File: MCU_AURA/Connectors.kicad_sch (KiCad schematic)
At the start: 13 parts, among them J500 Screw_Terminal_01x04, J501 TSW-108-07-G-T, J502 532617006, J504 532617004, J505 532617004, U500 DMN6040SSD-13

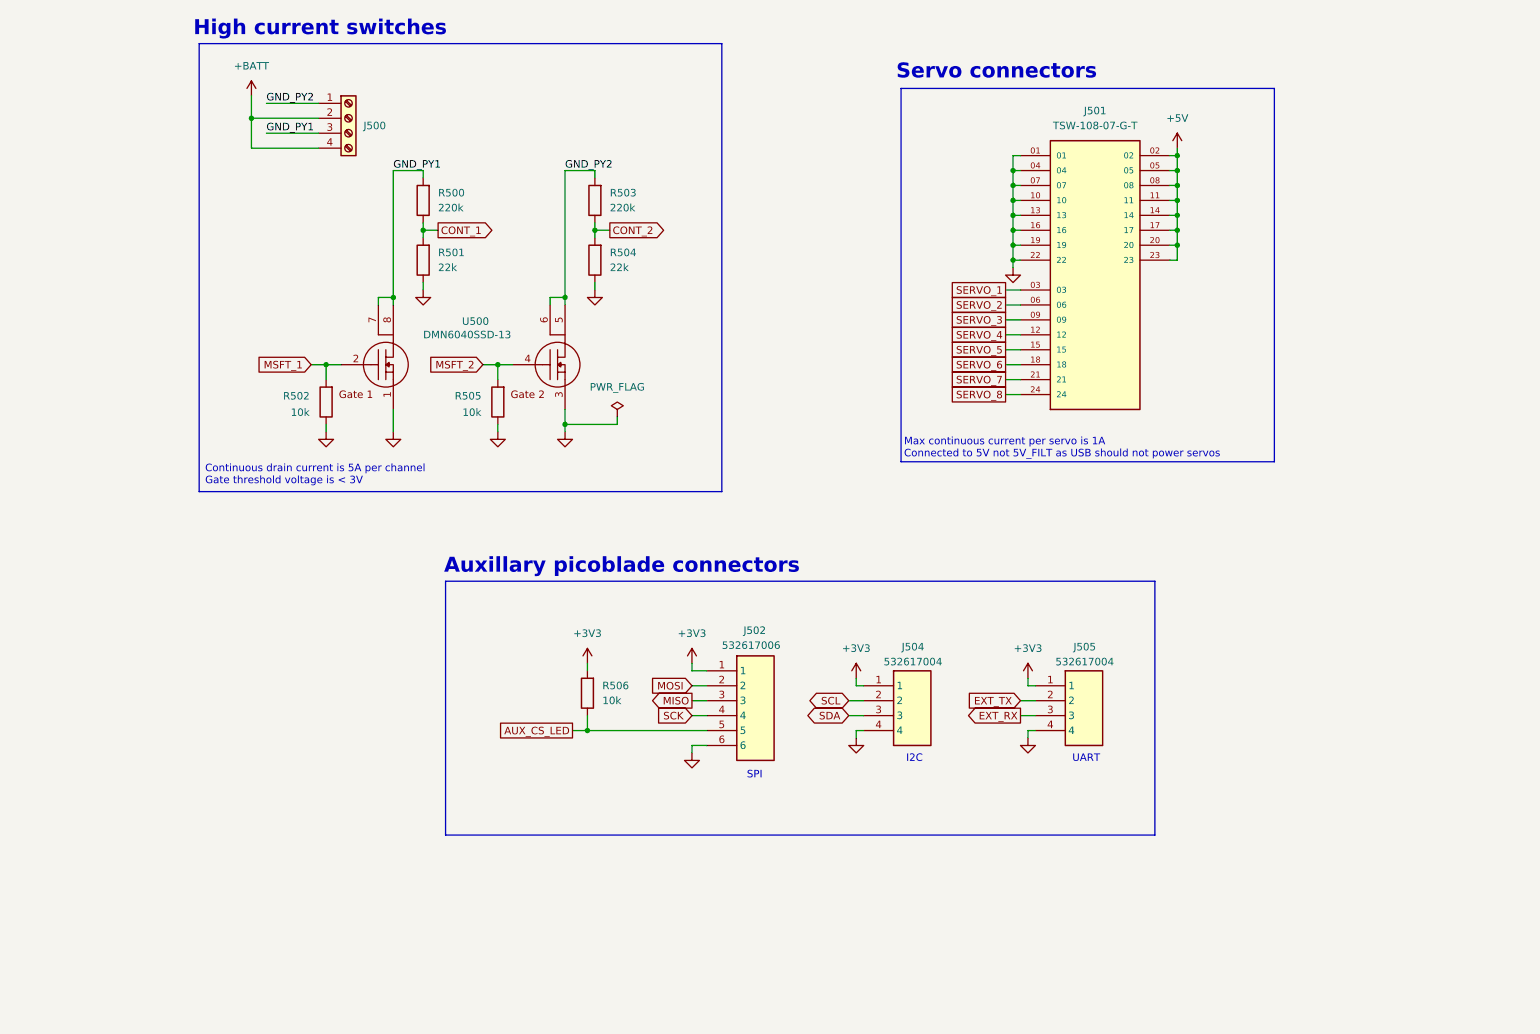
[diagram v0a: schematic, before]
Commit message: Started Editing
Problem syncing desktop to laptop (libraries).
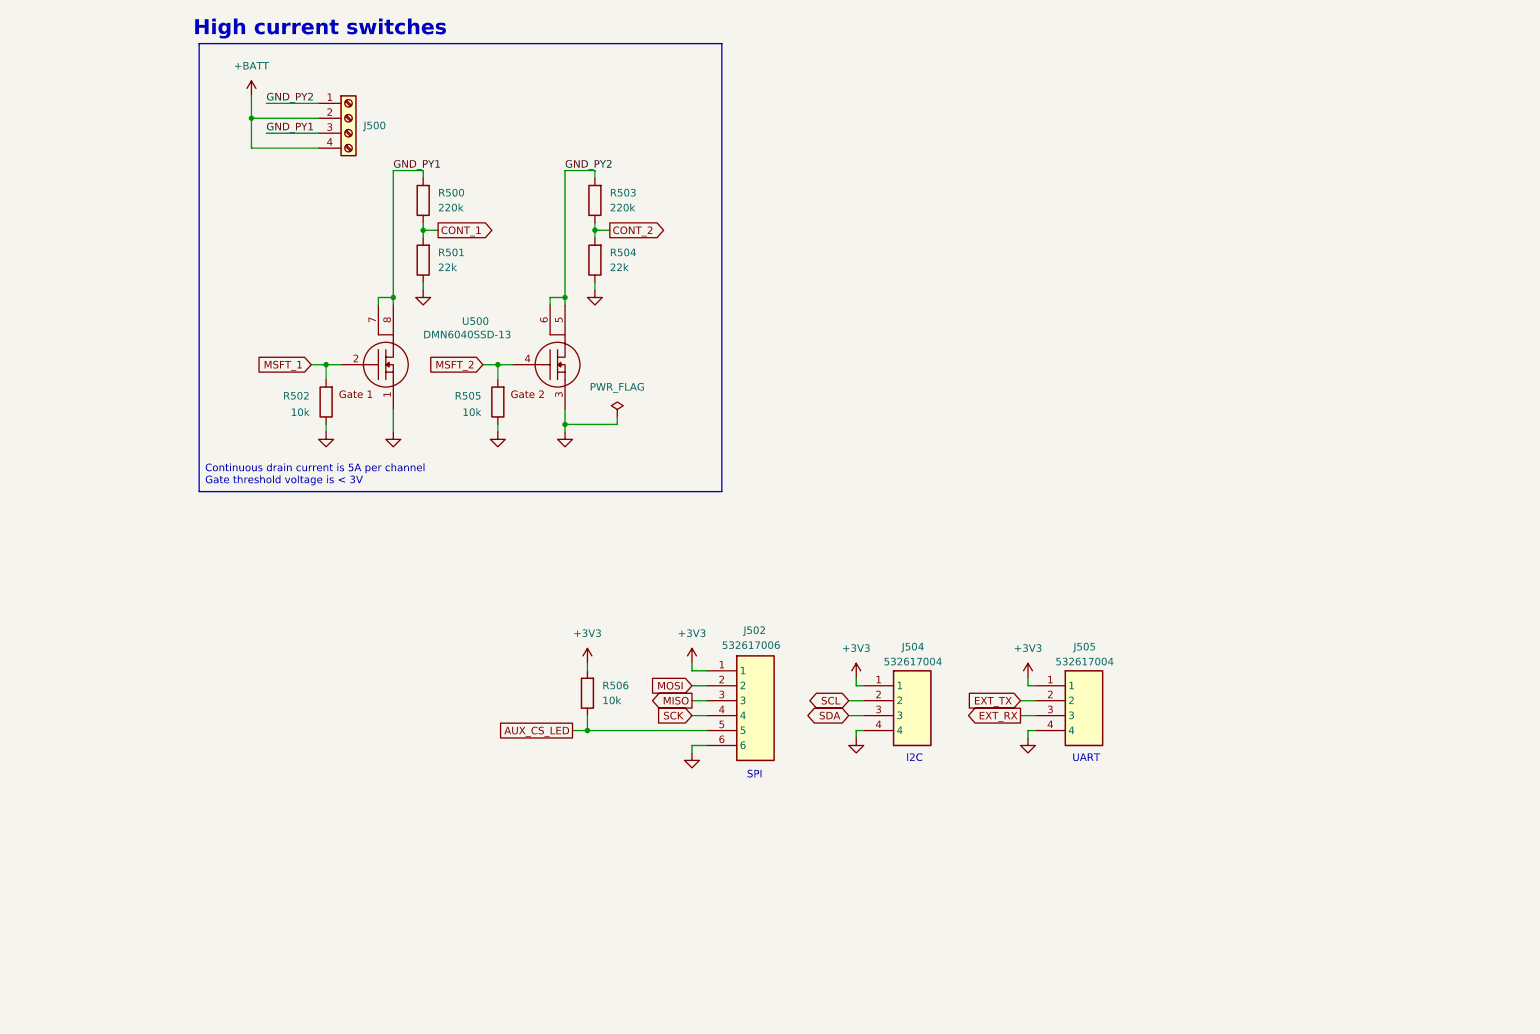
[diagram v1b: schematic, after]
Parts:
- removed J501: TSW-108-07-G-T, SAMTEC_TSW-108-07-G-T:SAMTEC_TSW-108-07-G-T, symbol TSW-108-07-G-T:TSW-108-07-G-T
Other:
- note removed: "Auxillary picoblade connectors"
- note removed: "Max continuous current per servo is 1A Connected to 5V not 5V_FILT as USB should not power servos"
- note removed: "Servo connectors"

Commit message: Added Samacsys libraries
Made the libraries from the component search engine local.
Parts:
- J502: footprint SamacSys_Parts:532617006 -> 532617006:532617006
- J504, J505: footprint SamacSys_Parts:532617004 -> 532617004:532617004
- U500: footprint SamacSys_Parts:SOIC127P600X170-8N -> DMN6040SSD-13:SOIC127P600X170-8N

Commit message: Synchronised
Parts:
- removed J502: 532617006, 532617006:532617006, symbol SamacSys_Parts:532617006
- removed J504, J505: 532617004, 532617004:532617004, symbol SamacSys_Parts:532617004
- removed U500: DMN6040SSD-13, DMN6040SSD-13:SOIC127P600X170-8N, symbol SamacSys_Parts:DMN6040SSD-13
- added J4: 532617006, 532617006:532617006, symbol 532617006:532617006
- added J5, J6: 532617004, 532617004:532617004, symbol 532617004:532617004
- added U1: DMN6040SSD-13, DMN6040SSD-13:SOIC127P600X170-8N, symbol DMN6040SSD-13:DMN6040SSD-13
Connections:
- net +3V3: now also J4.1, J5.1, J6.1
- net AUX_CS_LED: now also J4.5
- net EXT_RX: now also J6.3
- net EXT_TX: now also J6.2
- net GND: now also J4.6, J5.4, J6.4, U1.1, U1.3
- net GND_PY1: now also U1.7, U1.8
- net GND_PY2: now also U1.5, U1.6
- net MISO: now also J4.3
- net MOSI: now also J4.2
- net MSFT_1: now also U1.2
- net MSFT_2: now also U1.4
- net SCK: now also J4.4
- net SCL: now also J5.2
- net SDA: now also J5.3
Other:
- moved on the sheet: R506

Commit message: Adding Connectors
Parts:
- removed J4: 532617006, 532617006:532617006, symbol 532617006:532617006
- added J4, J8: 532617007, 532617007:532617007, symbol 532617007:532617007
- added J7: 532614005, 532614005:CONN_532610000-SD_05_MOL, symbol 532614005:532614005
- added J9: 532617004, 532617004:532617004, symbol 532617004:532617004
- added R1: 10k, Resistor_SMD:R_0402_1005Metric, symbol Device:R
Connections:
- net +3V3: now also J4.1, J7.1, J8.1, J9.1, R1.2
- net GND: now also J4.7, J7.5, J8.7, J9.4
- net MISO: now also J4.3, J8.3
- net MOSI: now also J4.2, J8.2
- net SCK: now also J4.4, J8.4
- net SCL: now also J9.2
- net SDA: now also J9.3
- net AUX_CS_LED renamed EXT_CS
- net EXT_CS: now also J4.5
- new net EXT_RST: J4.6
- new net GPS_INT: J7.4
- new net GPS_RX: J7.3
- new net GPS_TX: J7.2
- new net RF_CS: J8.5, R1.1
- new net RF_RST: J8.6
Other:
- note added: "GPS Connector"
- note added: "High power switches"
- note added: "I2C Connectors"
- note added: "RF Connector"
- note added: "SPI Connector"
- note added: "UART Connector"
- note removed: "High current switches"
- note removed: "SPI"
- note removed: "UART"
- moved on the sheet: J5, J500, J6, R500, R501, R502, R503, R504, R505, R506, U1

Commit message: Initial Schematic Draft
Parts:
- removed J500: Screw_Terminal_01x04, TerminalBlock_MetzConnect:TerminalBlock_MetzConnect_Type086_RT03404HBLC_1x04_P3.81mm_Horizontal, symbol Connector:Screw_Terminal_01x04
- removed R500, R503: 220k, Resistor_SMD:R_0402_1005Metric, symbol Device:R
- removed R501, R504: 22k, Resistor_SMD:R_0402_1005Metric, symbol Device:R
- removed R502, R505: 10k, Resistor_SMD:R_0402_1005Metric, symbol Device:R
- removed U1: DMN6040SSD-13, DMN6040SSD-13:SOIC127P600X170-8N, symbol DMN6040SSD-13:DMN6040SSD-13
- added J403: 532617010, 532617010:532617010, symbol 532617010:532617010
- added J406: 532617012, 532617012:532617012, symbol 532617012:532617012
- renumbered J5 to J400, J9 to J401, J6 to J402, J8 to J404, J4 to J405, J7 to J407, R1 to R400, R506 to R401
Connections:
- net +3V3: now also J403.3
- net GND: now also J403.10, J403.6, J403.9
- net MSFT_1: now also J403.7
- net MSFT_2: now also J403.8
- net SCL: now also J403.4
- net SDA: now also J403.5
- new net +5V: J403.1, J403.2
- new net SERVO_1: J406.1
- new net SERVO_10: J406.10
- new net SERVO_11: J406.11
- new net SERVO_12: J406.12
- new net SERVO_2: J406.2
- new net SERVO_3: J406.3
- new net SERVO_4: J406.4
- new net SERVO_5: J406.5
- new net SERVO_6: J406.6
- new net SERVO_7: J406.7
- new net SERVO_8: J406.8
- new net SERVO_9: J406.9
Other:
- note added: "PDB Connector"
- note added: "Servo Outputs"
- note removed: "Continuous drain current is 5A per channel Gate threshold voltage is < 3V"
- note removed: "High power switches"
- moved on the sheet: J400, J401, J402, J404, J405, J407, R400, R401

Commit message: Started Routing
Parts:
- removed J403: 532617010, 532617010:532617010, symbol 532617010:532617010
- removed J407: 532614005, 532614005:CONN_532610000-SD_05_MOL, symbol 532614005:532614005
- added C400: 10u, Capacitor_SMD:C_0402_1005Metric, symbol Device:C
- added C401: 1u, Capacitor_SMD:C_0402_1005Metric, symbol Device:C
- added C402: 100n, Capacitor_SMD:C_0402_1005Metric, symbol Device:C
- added D400, D401, D402, D403, D404, D405, D406, D407, D408, D409, D410: TPD1E05U06DPYR, TPD1E05U06DPYR:DIO_TPD1E05U06DPYR, symbol ESDALC5_1BM2:ESDALC5-1BM2
- added J403: 532617012, 532611271:53261-1271, symbol 532617012:532617012
- added J407: 532617007, 532610771:532610771, symbol 532617007:532617007
- added J408: 532617004, 532610471:53261-0471, symbol 532617004:532617004
- J400, J401, J402: footprint 532617004:532617004 -> 532610471:53261-0471
- J404, J405: footprint 532617007:532617007 -> 532610771:532610771
- J406: footprint 532617012:532617012 -> 532611271:53261-1271
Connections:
- net +3V3: now also D401.1, J403.4, J407.1, J407.2, J408.1
- net +5V: now also C400.1, C401.1, C402.1, D400.1, J403.10, J403.11, J403.12
- net EXT_RX: now also D408.1
- net EXT_TX: now also D407.1
- net GND: now also C400.2, C401.2, C402.2, D400.2, D401.2, D402.2, D403.2, D404.2, D405.2, D406.2, D407.2, D408.2, D409.2, D410.2, J403.1, J403.2, J403.3, J403.7, J407.6, J407.7, J408.3, J408.4
- net GPS_INT: now also D406.1, J407.5
- net GPS_RX: now also D405.1, J407.4
- net GPS_TX: now also D404.1, J407.3
- net MSFT_1: now also J403.8
- net MSFT_2: now also J403.9
- net SCL: now also D403.1, D409.1, J403.6
- net SDA: now also D402.1, D410.1, J403.5
- new net RC_RX: J408.2
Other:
- note added: "As both connectors are stacked, they share the TVS diodes for ESD protection"
- note removed: "I2C"
- moved on the sheet: J400, J402, J404, J405, J406, R400, R401

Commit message: Second Iteration MCU
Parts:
- renumbered J401 to J400, J400 to J401
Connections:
- net SCL: no longer J400.2
- net SDA: no longer J400.3
- new net CANH: J400.3
- new net CANL: J400.2
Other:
- note added: "CAN Connector"
- note added: "ESD protection built into CAN transceiver."
- note added: "I2C Connector"
- note added: "RC Connector"
- note removed: "As both connectors are stacked, they share the TVS diodes for ESD protection"
- note removed: "I2C Connectors"
- moved on the sheet: D404, D405, D406, D409, D410, J400, J401, J406, J407, J408

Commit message: Production Files for MCU
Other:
- moved on the sheet: C400, C401
